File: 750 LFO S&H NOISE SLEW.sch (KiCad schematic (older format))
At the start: 236 parts, among them J1 JACK_MONO_SW, J10 JACK_MONO_SW, J11 JACK_MONO_SW, J2 JACK_MONO_SW, J3 JACK_MONO_SW, J4 JACK_MONO_SW, J5 JACK_MONO_SW, J6 JACK_MONO_SW, J7 JACK_MONO_SW, J8 JACK_MONO_SW, J9 JACK_MONO_SW, P1 CONN_02X01, P2 CONN_02X01, P3 CONN_02X05, Q1 MMBT3904, Q10 MMBT3904, Q11 J112, Q12 MMBT3906, Q13 J112, Q14 J112, Q15 MMBT3904, Q16 MMBT3904, Q2 MMBT3904, Q3 2N7002, Q4 2N7002, Q5 MBT3946DW, Q6 DMMT3904W, Q7 MMBT3904, Q8 MMBT3904, Q9 MMBT3904, SW1 KS-01Q, SW2 KS-01Q, U1 LM13700, U10 TL072-, U11 TL072-, U12 MAX9945, U13 DG409, U14 DG409, U2 TL072-, U3 TL072-, U4 TL072-, U5 TL072-, U6 CD40106, U7 CD4027, U8 CD4027, U9 TL072-

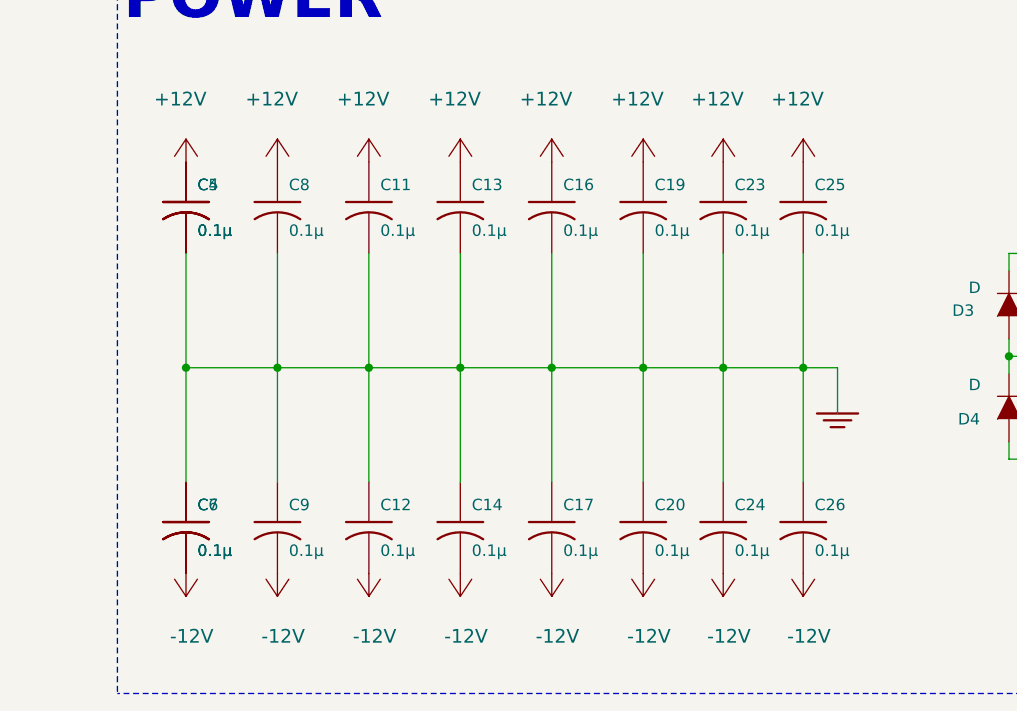
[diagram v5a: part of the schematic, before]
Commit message: routing power and ground, all components placed
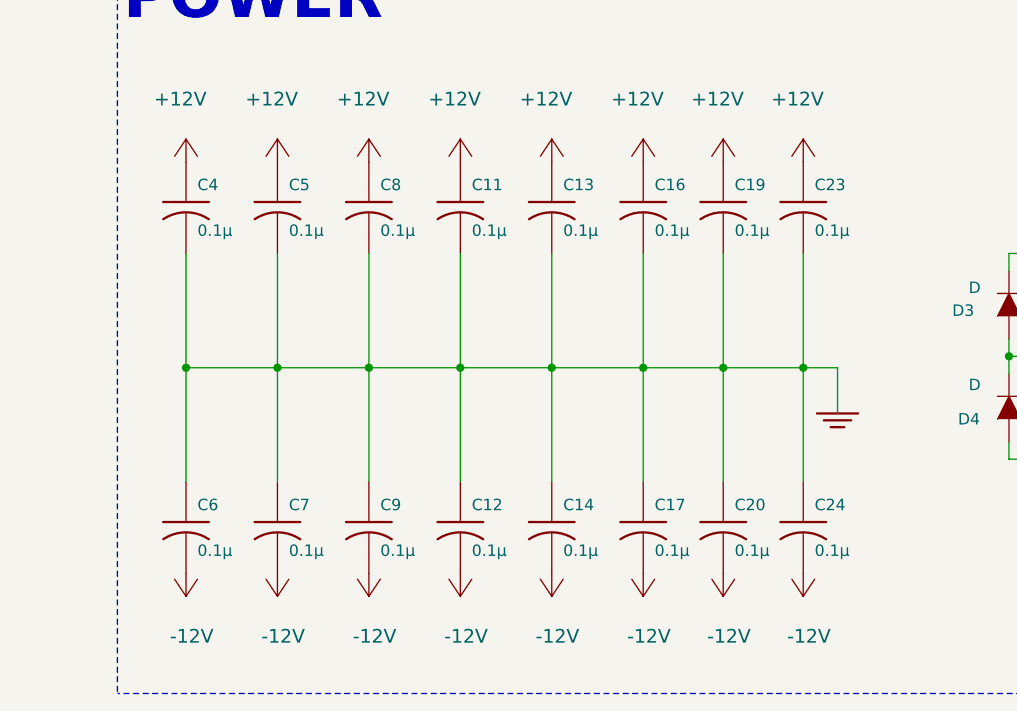
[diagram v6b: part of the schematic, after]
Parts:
- removed C25, C26: 0.1µ, MyModules:SM0603-C-JRL, symbol C_US
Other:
- moved on the sheet: C11, C12, C13, C14, C16, C17, C19, C20, C23, C24, C5, C7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
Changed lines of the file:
@@
 L C_US C8
 U 1 1 56E5AE7D
-P 2900 18700
-F 0 "C8" H 2950 18800 50  0000 L CNN
-F 1 "0.1µ" H 2950 18600 50  0000 L CNN
-F 2 "MyModules:SM0603-C-JRL" H 2900 18700 60  0001 C CNN
-F 3 "~" H 2900 18700 60  0000 C CNN
-	1    2900 18700
+P 3300 18700
+F 0 "C8" H 3350 18800 50  0000 L CNN
+F 1 "0.1µ" H 3350 18600 50  0000 L CNN
+F 2 "MyModules:SM0603-C-JRL" H 3300 18700 60  0001 C CNN
+F 3 "~" H 3300 18700 60  0000 C CNN
+	1    3300 18700
 	1    0    0    -1
 $EndComp
@@
 L C_US C11
 U 1 1 56E5AE7F
-P 3300 18700
-F 0 "C11" H 3350 18800 50  0000 L CNN
-F 1 "0.1µ" H 3350 18600 50  0000 L CNN
-F 2 "MyModules:SM0603-C-JRL" H 3300 18700 60  0001 C CNN
-F 3 "~" H 3300 18700 60  0000 C CNN
-	1    3300 18700
+P 3700 18700
+F 0 "C11" H 3750 18800 50  0000 L CNN
+F 1 "0.1µ" H 3750 18600 50  0000 L CNN
+F 2 "MyModules:SM0603-C-JRL" H 3700 18700 60  0001 C CNN
+F 3 "~" H 3700 18700 60  0000 C CNN
+	1    3700 18700
 	1    0    0    -1
 $EndComp
@@
 L C_US C19
 U 1 1 56E5AE81
-P 4500 18700
-F 0 "C19" H 4550 18800 50  0000 L CNN
-F 1 "0.1µ" H 4550 18600 50  0000 L CNN
-F 2 "MyModules:SM0603-C-JRL" H 4500 18700 60  0001 C CNN
-F 3 "~" H 4500 18700 60  0000 C CNN
-	1    4500 18700
+P 4850 18700
+F 0 "C19" H 4900 18800 50  0000 L CNN
+F 1 "0.1µ" H 4900 18600 50  0000 L CNN
+F 2 "MyModules:SM0603-C-JRL" H 4850 18700 60  0001 C CNN
+F 3 "~" H 4850 18700 60  0000 C CNN
+	1    4850 18700
 	1    0    0    -1
 $EndComp
@@
 L C_US C23
 U 1 1 56E5AE83
-P 4850 18700
-F 0 "C23" H 4900 18800 50  0000 L CNN
-F 1 "0.1µ" H 4900 18600 50  0000 L CNN
-F 2 "MyModules:SM0603-C-JRL" H 4850 18700 60  0001 C CNN
-F 3 "~" H 4850 18700 60  0000 C CNN
-	1    4850 18700
+P 5200 18700
+F 0 "C23" H 5250 18800 50  0000 L CNN
+F 1 "0.1µ" H 5250 18600 50  0000 L CNN
+F 2 "MyModules:SM0603-C-JRL" H 5200 18700 60  0001 C CNN
+F 3 "~" H 5200 18700 60  0000 C CNN
+	1    5200 18700
 	1    0    0    -1
 $EndComp
@@
 L C_US C13
 U 1 1 56E5AE85
-P 3700 18700
-F 0 "C13" H 3750 18800 50  0000 L CNN
-F 1 "0.1µ" H 3750 18600 50  0000 L CNN
-F 2 "MyModules:SM0603-C-JRL" H 3700 18700 60  0001 C CNN
-F 3 "~" H 3700 18700 60  0000 C CNN
-	1    3700 18700
+P 4100 18700
+F 0 "C13" H 4150 18800 50  0000 L CNN
+F 1 "0.1µ" H 4150 18600 50  0000 L CNN
+F 2 "MyModules:SM0603-C-JRL" H 4100 18700 60  0001 C CNN
+F 3 "~" H 4100 18700 60  0000 C CNN
+	1    4100 18700
 	1    0    0    -1
 $EndComp
@@
 L C_US C16
 U 1 1 56E5AE87
-P 4100 18700
-F 0 "C16" H 4150 18800 50  0000 L CNN
-F 1 "0.1µ" H 4150 18600 50  0000 L CNN
-F 2 "MyModules:SM0603-C-JRL" H 4100 18700 60  0001 C CNN
-F 3 "~" H 4100 18700 60  0000 C CNN
-	1    4100 18700
+P 4500 18700
+F 0 "C16" H 4550 18800 50  0000 L CNN
+F 1 "0.1µ" H 4550 18600 50  0000 L CNN
+F 2 "MyModules:SM0603-C-JRL" H 4500 18700 60  0001 C CNN
+F 3 "~" H 4500 18700 60  0000 C CNN
+	1    4500 18700
 	1    0    0    -1
 $EndComp
@@
 L C_US C9
 U 1 1 56E5AE89
-P 2900 20100
-F 0 "C9" H 2950 20200 50  0000 L CNN
-F 1 "0.1µ" H 2950 20000 50  0000 L CNN
-F 2 "MyModules:SM0603-C-JRL" H 2900 20100 60  0001 C CNN
-F 3 "~" H 2900 20100 60  0000 C CNN
-	1    2900 20100
+P 3300 20100
+F 0 "C9" H 3350 20200 50  0000 L CNN
+F 1 "0.1µ" H 3350 20000 50  0000 L CNN
+F 2 "MyModules:SM0603-C-JRL" H 3300 20100 60  0001 C CNN
+F 3 "~" H 3300 20100 60  0000 C CNN
+	1    3300 20100
 	1    0    0    -1
 $EndComp
@@
 L C_US C12
 U 1 1 56E5AE8B
-P 3300 20100
-F 0 "C12" H 3350 20200 50  0000 L CNN
-F 1 "0.1µ" H 3350 20000 50  0000 L CNN
-F 2 "MyModules:SM0603-C-JRL" H 3300 20100 60  0001 C CNN
-F 3 "~" H 3300 20100 60  0000 C CNN
-	1    3300 20100
+P 3700 20100
+F 0 "C12" H 3750 20200 50  0000 L CNN
+F 1 "0.1µ" H 3750 20000 50  0000 L CNN
+F 2 "MyModules:SM0603-C-JRL" H 3700 20100 60  0001 C CNN
+F 3 "~" H 3700 20100 60  0000 C CNN
+	1    3700 20100
 	1    0    0    -1
 $EndComp
@@
 L C_US C20
 U 1 1 56E5AE8D
-P 4500 20100
-F 0 "C20" H 4550 20200 50  0000 L CNN
-F 1 "0.1µ" H 4550 20000 50  0000 L CNN
-F 2 "MyModules:SM0603-C-JRL" H 4500 20100 60  0001 C CNN
-F 3 "~" H 4500 20100 60  0000 C CNN
-	1    4500 20100
+P 4850 20100
+F 0 "C20" H 4900 20200 50  0000 L CNN
+F 1 "0.1µ" H 4900 20000 50  0000 L CNN
+F 2 "MyModules:SM0603-C-JRL" H 4850 20100 60  0001 C CNN
+F 3 "~" H 4850 20100 60  0000 C CNN
+	1    4850 20100
 	1    0    0    -1
 $EndComp
@@
 L C_US C24
 U 1 1 56E5AE8F
-P 4850 20100
-F 0 "C24" H 4900 20200 50  0000 L CNN
-F 1 "0.1µ" H 4900 20000 50  0000 L CNN
-F 2 "MyModules:SM0603-C-JRL" H 4850 20100 60  0001 C CNN
-F 3 "~" H 4850 20100 60  0000 C CNN
-	1    4850 20100
+P 5200 20100
+F 0 "C24" H 5250 20200 50  0000 L CNN
+F 1 "0.1µ" H 5250 20000 50  0000 L CNN
+F 2 "MyModules:SM0603-C-JRL" H 5200 20100 60  0001 C CNN
+F 3 "~" H 5200 20100 60  0000 C CNN
+	1    5200 20100
 	1    0    0    -1
 $EndComp
@@
 L C_US C14
 U 1 1 56E5AE91
-P 3700 20100
-F 0 "C14" H 3750 20200 50  0000 L CNN
-F 1 "0.1µ" H 3750 20000 50  0000 L CNN
-F 2 "MyModules:SM0603-C-JRL" H 3700 20100 60  0001 C CNN
-F 3 "~" H 3700 20100 60  0000 C CNN
-	1    3700 20100
+P 4100 20100
+F 0 "C14" H 4150 20200 50  0000 L CNN
+F 1 "0.1µ" H 4150 20000 50  0000 L CNN
+F 2 "MyModules:SM0603-C-JRL" H 4100 20100 60  0001 C CNN
+F 3 "~" H 4100 20100 60  0000 C CNN
+	1    4100 20100
 	1    0    0    -1
 $EndComp
@@
 L C_US C17
 U 1 1 56E5AE93
-P 4100 20100
-F 0 "C17" H 4150 20200 50  0000 L CNN
-F 1 "0.1µ" H 4150 20000 50  0000 L CNN
-F 2 "MyModules:SM0603-C-JRL" H 4100 20100 60  0001 C CNN
-F 3 "~" H 4100 20100 60  0000 C CNN
-	1    4100 20100
+P 4500 20100
+F 0 "C17" H 4550 20200 50  0000 L CNN
+F 1 "0.1µ" H 4550 20000 50  0000 L CNN
+F 2 "MyModules:SM0603-C-JRL" H 4500 20100 60  0001 C CNN
+F 3 "~" H 4500 20100 60  0000 C CNN
+	1    4500 20100
 	1    0    0    -1
 $EndComp
@@
 L C_US C5
 U 1 1 56E5AE98
-P 2500 18700
-F 0 "C5" H 2550 18800 50  0000 L CNN
-F 1 "0.1µ" H 2550 18600 50  0000 L CNN
-F 2 "MyModules:SM0603-C-JRL" H 2500 18700 60  0001 C CNN
-F 3 "~" H 2500 18700 60  0000 C CNN
-	1    2500 18700
+P 2900 18700
+F 0 "C5" H 2950 18800 50  0000 L CNN
+F 1 "0.1µ" H 2950 18600 50  0000 L CNN
+F 2 "MyModules:SM0603-C-JRL" H 2900 18700 60  0001 C CNN
+F 3 "~" H 2900 18700 60  0000 C CNN
+	1    2900 18700
 	1    0    0    -1
 $EndComp
@@
 L C_US C7
 U 1 1 56E5AE9C
-P 2500 20100
-F 0 "C7" H 2550 20200 50  0000 L CNN
-F 1 "0.1µ" H 2550 20000 50  0000 L CNN
-F 2 "MyModules:SM0603-C-JRL" H 2500 20100 60  0001 C CNN
-F 3 "~" H 2500 20100 60  0000 C CNN
-	1    2500 20100
+P 2900 20100
+F 0 "C7" H 2950 20200 50  0000 L CNN
+F 1 "0.1µ" H 2950 20000 50  0000 L CNN
+F 2 "MyModules:SM0603-C-JRL" H 2900 20100 60  0001 C CNN
+F 3 "~" H 2900 20100 60  0000 C CNN
+	1    2900 20100
 	1    0    0    -1
 $EndComp
@@
 $EndComp
 $Comp
-L C_US C25
-U 1 1 56E5AE9E
-P 5200 18700
-F 0 "C25" H 5250 18800 50  0000 L CNN
-F 1 "0.1µ" H 5250 18600 50  0000 L CNN
-F 2 "MyModules:SM0603-C-JRL" H 5200 18700 60  0001 C CNN
-F 3 "~" H 5200 18700 60  0000 C CNN
-	1    5200 18700
-	1    0    0    -1
-$EndComp
-$Comp
 L +12V #PWR016
 U 1 1 56E5AE9F
@@
 	1    0    0    -1
 $EndComp
-$Comp
-L C_US C26
-U 1 1 56E5AEA0
-P 5200 20100
-F 0 "C26" H 5250 20200 50  0000 L CNN
-F 1 "0.1µ" H 5250 20000 50  0000 L CNN
-F 2 "MyModules:SM0603-C-JRL" H 5200 20100 60  0001 C CNN
-F 3 "~" H 5200 20100 60  0000 C CNN
-	1    5200 20100
-	1    0    0    -1
-$EndComp

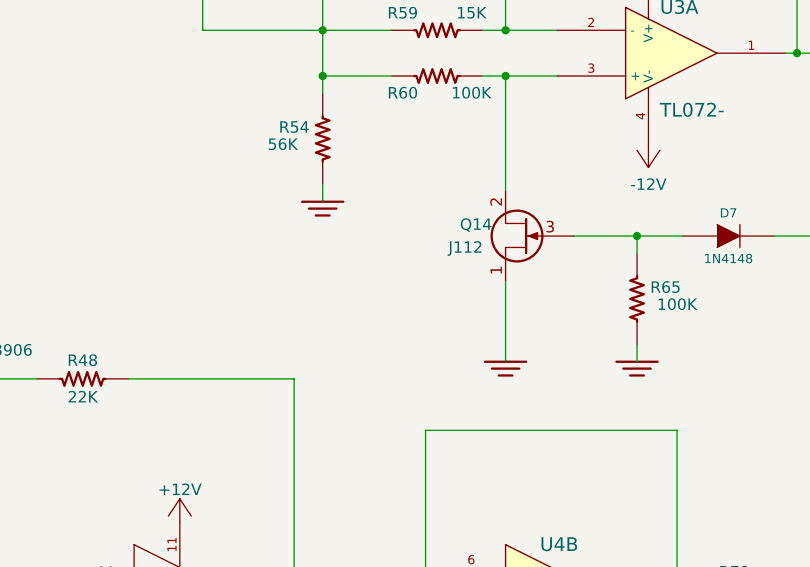
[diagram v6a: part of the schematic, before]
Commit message: adjust silkscreen
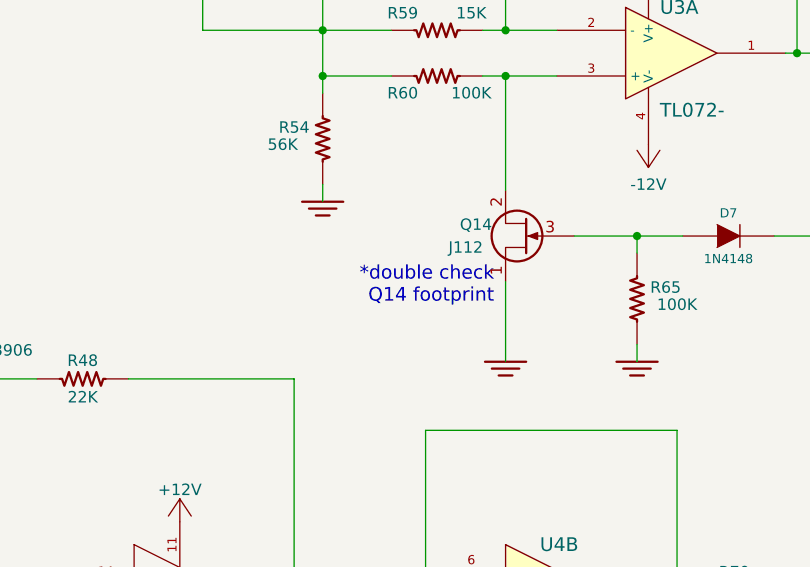
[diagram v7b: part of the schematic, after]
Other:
- note added: "*double check\nQ14 footprint"
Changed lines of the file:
@@
 Wire Wire Line
 	6825 2700 6950 2700
+Text Notes 10150 13600 2    60   ~ 0
+*double check\nQ14 footprint
 $EndSCHEMATC
